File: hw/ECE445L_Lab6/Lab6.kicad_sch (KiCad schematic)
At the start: 36 parts, among them J1 JST1.25, J3 Speaker, J4 Debugger, J5 ZX62D-B-5PA8_30_, J6 Header2, J7 Testpoints, SW1 RST, SW2 Mode, SW3 Mode, SW4 Mode, SW5 Mode, U1 Adafruit ST7735R, U2 LP2950-33LPRE3, U3 M0G3507QDGS32RQ1, Y1 16MHz

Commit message: updates thus far
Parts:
- added IC1: AD8300ARZ, SOIC127P600X175-8N, symbol lab6_symbols:AD8300ARZ
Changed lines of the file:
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@@
+	)
+	(symbol
+		(lib_id "lab6_symbols:AD8300ARZ")
+		(at 66.04 125.73 0)
+		(unit 1)
+		(body_style 1)
+		(exclude_from_sim no)
+		(in_bom yes)
+		(on_board yes)
+		(in_pos_files yes)
+		(dnp no)
+		(fields_autoplaced yes)
+		(property "Reference" "IC1"
+			(at 80.01 118.11 0)
+			(show_name no)
+			(do_not_autoplace no)
+			(effects
+				(font
+					(size 1.27 1.27)
+				)
+			)
+		)
+		(property "Value" "AD8300ARZ"
+			(at 80.01 120.65 0)
+			(show_name no)
+			(do_not_autoplace no)
+			(effects
+				(font
+					(size 1.27 1.27)
+				)
+			)
+		)
+		(property "Footprint" "SOIC127P600X175-8N"
+			(at 90.17 220.65 0)
+			(hide yes)
+			(show_name no)
+			(do_not_autoplace no)
+			(effects
+				(font
+					(size 1.27 1.27)
+				)
+				(justify left top)
+			)
+		)
+		(property "Datasheet" "https://datasheet.datasheetarchive.com/originals/distributors/Datasheets-4/DSA-70310.pdf"
+			(at 90.17 320.65 0)
+			(hide yes)
+			(show_name no)
+			(do_not_autoplace no)
+			(effects
+				(font
+					(size 1.27 1.27)
+				)
+				(justify left top)
+			)
+		)
+		(property "Description" "DAC 1-Ch R-2R 12-Bit 8-Pin SOIC"
+			(at 66.04 125.73 0)
+			(hide yes)
+			(show_name no)
+			(do_not_autoplace no)
+			(effects
+				(font
+					(size 1.27 1.27)
+				)
+			)
+		)
+		(property "Height" "1.75"
+			(at 90.17 520.65 0)
+			(hide yes)
+			(show_name no)
+			(do_not_autoplace no)
+			(effects
+				(font
+					(size 1.27 1.27)
+				)
+				(justify left top)
+			)
+		)
+		(property "Manufacturer_Name" "Analog Devices"
+			(at 90.17 620.65 0)
+			(hide yes)
+			(show_name no)
+			(do_not_autoplace no)
+			(effects
+				(font
+					(size 1.27 1.27)
+				)
+				(justify left top)
+			)
+		)
+		(property "Manufacturer_Part_Number" "AD8300ARZ"
+			(at 90.17 720.65 0)
+			(hide yes)
+			(show_name no)
+			(do_not_autoplace no)
+			(effects
+				(font
+					(size 1.27 1.27)
+				)
+				(justify left top)
+			)
+		)
+		(property "Mouser Part Number" "584-AD8300ARZ"
+			(at 90.17 820.65 0)
+			(hide yes)
+			(show_name no)
+			(do_not_autoplace no)
+			(effects
+				(font
+					(size 1.27 1.27)
+				)
+				(justify left top)
+			)
+		)
+		(property "Mouser Price/Stock" "https://www.mouser.co.uk/ProductDetail/Analog-Devices/AD8300ARZ?qs=%2FtpEQrCGXCy4SzE5uMQsTQ%3D%3D"
+			(at 90.17 920.65 0)
+			(hide yes)
+			(show_name no)
+			(do_not_autoplace no)
+			(effects
+				(font
+					(size 1.27 1.27)
+				)
+				(justify left top)
+			)
+		)
+		(property "Arrow Part Number" "AD8300ARZ"
+			(at 90.17 1020.65 0)
+			(hide yes)
+			(show_name no)
+			(do_not_autoplace no)
+			(effects
+				(font
+					(size 1.27 1.27)
+				)
+				(justify left top)
+			)
+		)
+		(property "Arrow Price/Stock" "https://www.arrow.com/en/products/ad8300arz/analog-devices?utm_currency=USD&region=nac"
+			(at 90.17 1120.65 0)
+			(hide yes)
+			(show_name no)
+			(do_not_autoplace no)
+			(effects
+				(font
+					(size 1.27 1.27)
+				)
+				(justify left top)
+			)
+		)
+		(pin "8"
+		)
+		(pin "7"
+		)
+		(pin "2"
+		)
+		(pin "5"
+		)
+		(pin "6"
+		)
+		(pin "3"
+		)
+		(pin "1"
+		)
+		(pin "4"
+		)
+		(instances
+			(project "Lab6"
+				(path "/69b823fd-c065-40ff-9bb9-c5835555f3eb"
+					(reference "IC1")
+					(unit 1)
+				)
+			)
+		)
 	)
 	(symbol

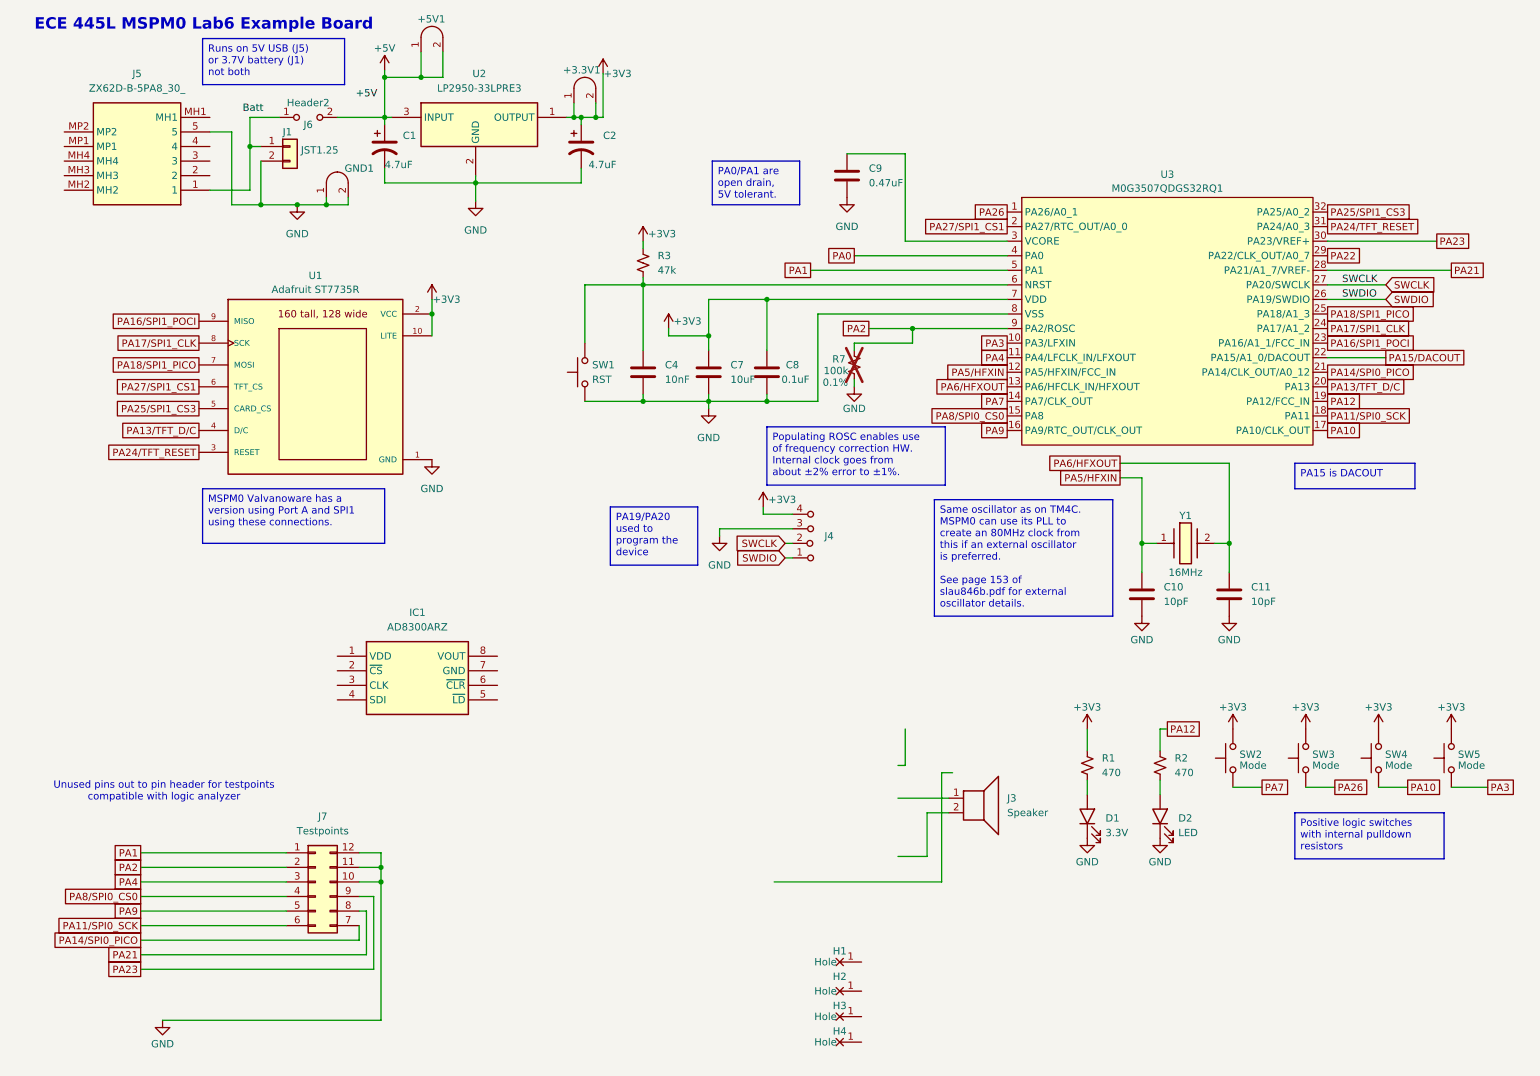
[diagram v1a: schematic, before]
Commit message: erc no errrors on schematic
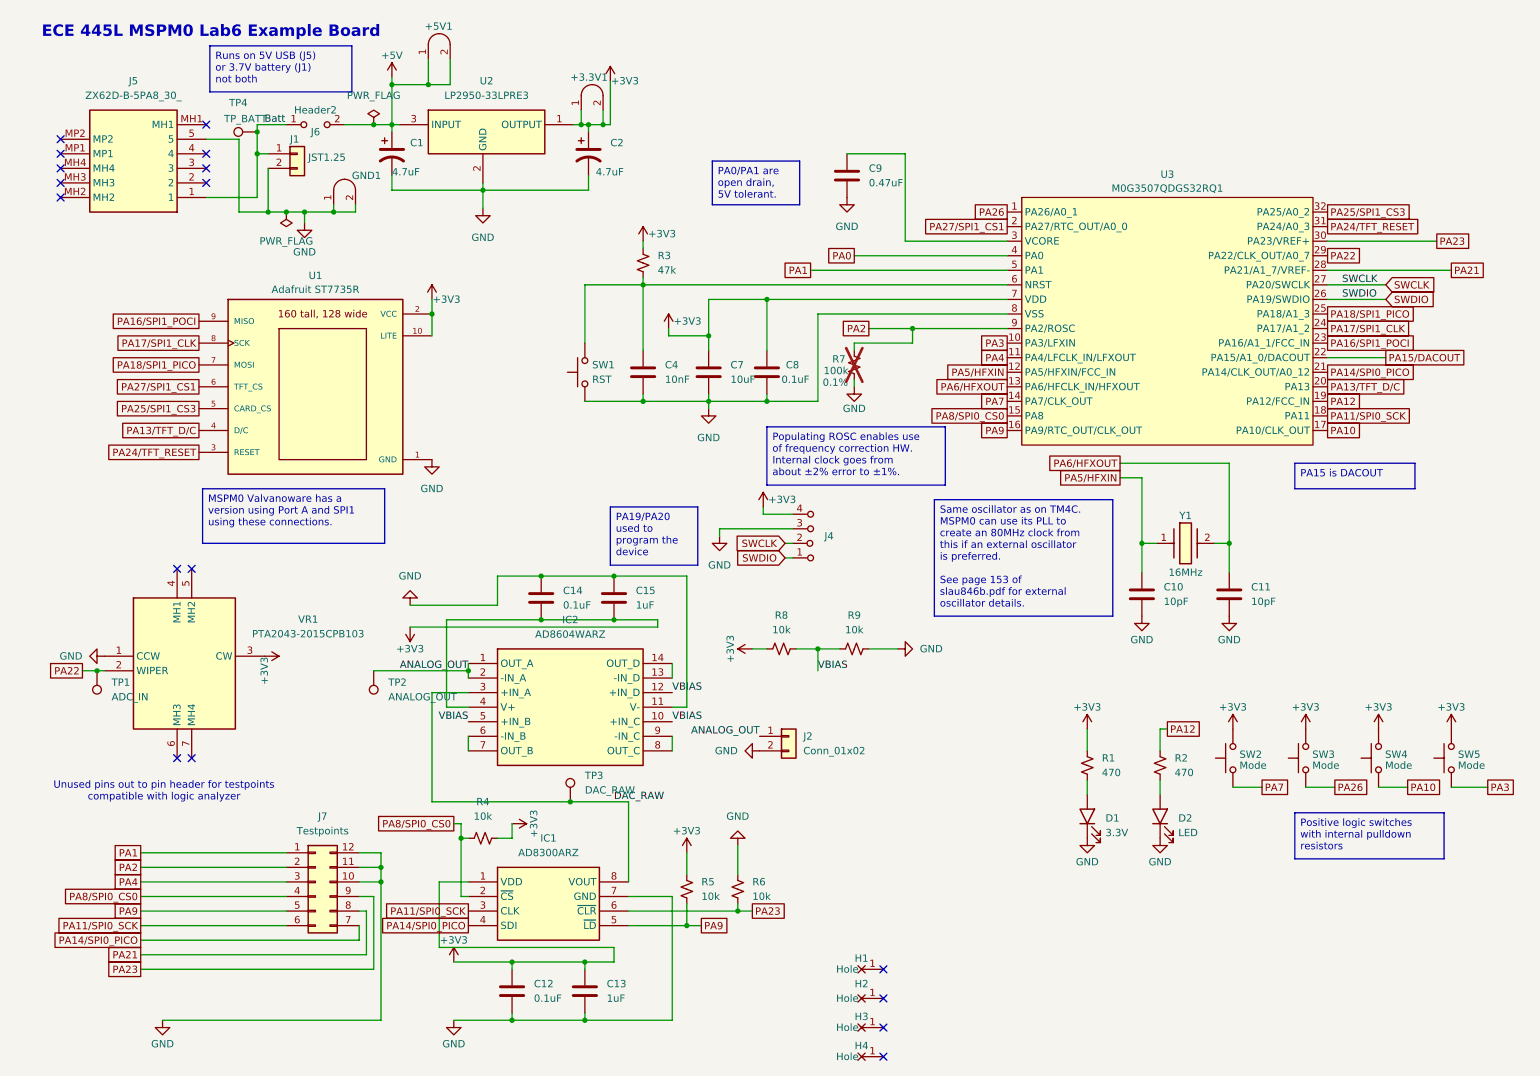
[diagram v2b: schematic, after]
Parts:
- removed J3: Speaker, Connector_PinHeader_2.54mm:PinHeader_1x02_P2.54mm_Vertical, symbol Device:Speaker
- added C12, C14: 0.1uF, ECE445L:C_Radial_100mil, symbol ECE445L:C
- added C13, C15: 1uF, ECE445L:C_Radial_100mil, symbol ECE445L:C
- added IC2: AD8604WARZ, SOP65P640X120-14N, symbol lab6_symbols:AD8604WARZ
- added J2: Conn_01x02, Connector_PinHeader_2.54mm:PinHeader_1x02_P2.54mm_Vertical, symbol Connector_Generic:Conn_01x02
- added R4, R5, R6, R8, R9: 10k, ECE445L:R_Axial_DIN0204_L3.6mm_D1.6mm_P7.62mm_Horizontal, symbol ECE445L:R_0.125W
- added TP1: ADC_IN, TestPoint:TestPoint_Pad_D2.0mm, symbol Connector:TestPoint
- added TP2: ANALOG_OUT, PTA20432015CPB103, symbol Connector:TestPoint
- added TP3: DAC_RAW, PTA20432015CPB103, symbol Connector:TestPoint
- added TP4: TP_BATT, TestPoint:TestPoint_THTPad_D2.0mm_Drill1.0mm, symbol Connector:TestPoint
- added VR1: PTA2043-2015CPB103, PTA20432015CPB103, symbol lab6_symbols:PTA2043-2015CPB103
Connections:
- net +3V3: now also IC1.1 (VDD), C12.1, C13.1, C14.2, C15.2, IC2.4 (V+), R4.1, R5.1, R8.1, VR1.3 (CW)
- net Batt: now also J1.1 (Pin_1), J5.1, J6.1 (A), TP4.1
- net GND: now also IC1.7 (GND), C12.2, C13.2, C14.1, C15.1, IC2.11 (V-), J2.2 (Pin_2), R6.1, R9.2, VR1.1 (CCW)
- net PA11/SPI0_SCK: now also IC1.3 (CLK)
- net PA14/SPI0_PICO: now also IC1.4 (SDI)
- net PA22: now also TP1.1, VR1.2 (WIPER)
- net PA23: now also IC1.6 (~{CLR}), R6.2
- net PA8/SPI0_CS0: now also IC1.2 (~{CS}), R4.2
- net PA9: now also IC1.5 (~{LD}), R5.2
- net DAC_RAW: now reaches IC1.8 (VOUT)
- net DAC_RAW: now also IC2.3 (+IN_A), TP3.1
- new net: IC2.13 (-IN_D), IC2.14 (OUT_D)
- new net: IC2.6 (-IN_B), IC2.7 (OUT_B)
- new net: IC2.8 (OUT_C), IC2.9 (-IN_C)
- new net ANALOG_OUT: IC2.1 (OUT_A), IC2.2 (-IN_A), J2.1 (Pin_1), TP2.1
- new net VBIAS: IC2.10 (+IN_C), IC2.12 (+IN_D), IC2.5 (+IN_B), R8.2, R9.1
- no-connect marks 0 -> 17
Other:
- moved on the sheet: +3.3V1, +5V1, C1, C2, GND1, H1, H2, H3, H4, IC1, J1, J5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

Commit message: before fixing all the off grid warnings
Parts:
- removed J4: Debugger, ECE445L:PinHeader_1x04_P2.54mm_Vertical, symbol ECE445L:Header_4
- C10, C11, C13, C15: footprint ECE445L:C_Radial_100mil -> Capacitor_THT:C_Rect_L4.0mm_W2.5mm_P2.50mm
- C12, C14, C7, C8: footprint ECE445L:C_Radial_100mil -> Capacitor_THT:C_Rect_L4.6mm_W3.8mm_P2.50mm_MKS02_FKP02
- C9: footprint ECE445L:C_Radial_100mil -> Capacitor_THT:C_Rect_L7.0mm_W3.5mm_P2.50mm_P5.00mm
- IC1: footprint SOIC127P600X175-8N -> ECE445L:SOIC127P600X175-8N
- IC2: footprint SOP65P640X120-14N -> Package_SO:SOIC-14_3.9x8.7mm_P1.27mm
- J1: footprint ECE445L:JST-1x02_1.25mm -> Connector_Molex:Molex_PicoBlade_53047-0210_1x02_P1.25mm_Vertical
- TP2, TP3: footprint PTA20432015CPB103 -> TestPoint:TestPoint_Pad_D2.0mm
- U3: footprint ECE445L:VSSOP_0.5mm_32pin_handsolder -> ECE445L:generic_VSSOP_0.5mm
- VR1: footprint PTA20432015CPB103 -> ECE445L:PTA20432015CPB103
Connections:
- no-connect marks 17 -> 19

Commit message: linking errors ignored and zero errors in pcb
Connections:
- no-connect marks 19 -> 21
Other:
- moved on the sheet: +3.3V1, +5V1, C1, C10, C11, C2, GND1, J1, U2, Y1
